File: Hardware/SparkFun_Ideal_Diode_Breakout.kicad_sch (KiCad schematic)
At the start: 23 parts, among them J1 Conn_01x05, J2 Conn_01x05, Q1 BCM857BS-7-F, Q2 DMG2305UX, Q3 BCM857BS-7-F, Q4 DMG2305UX, Q5 BCM857BS-7-F, Q6 DMG2305UX, Q7 BCM857BS-7-F, Q8 DMG2305UX

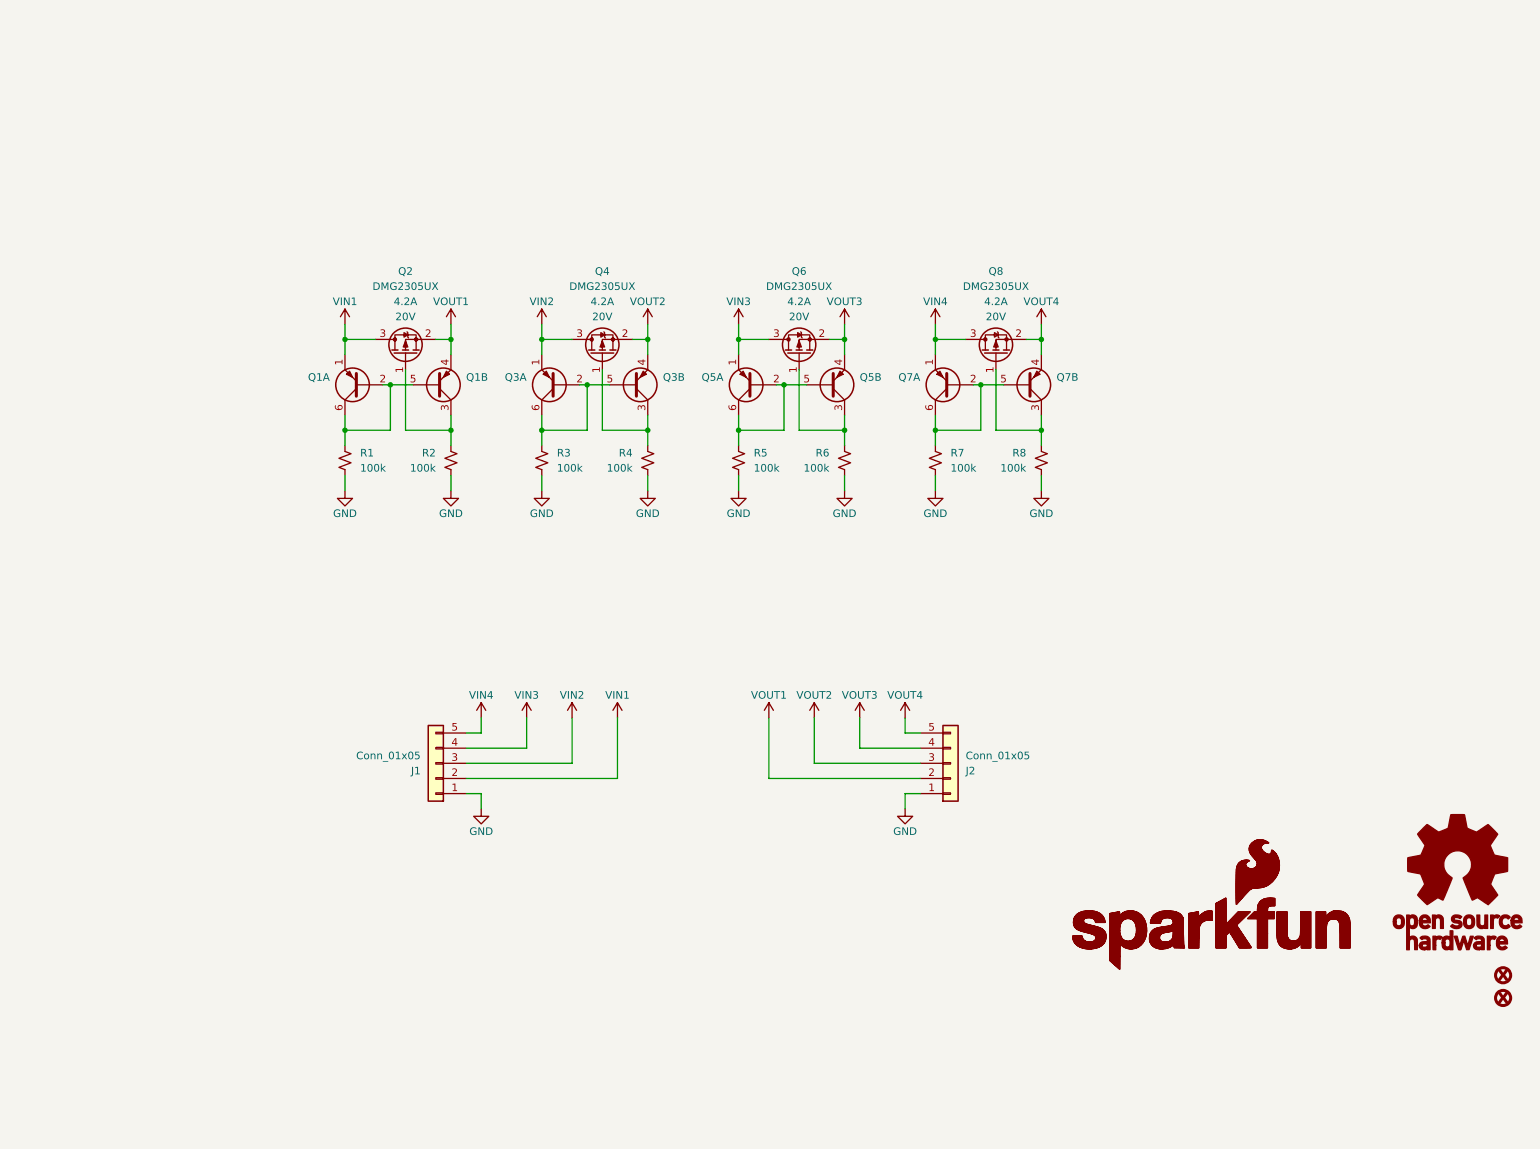
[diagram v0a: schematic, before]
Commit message: Design review updates
Update page info on schematic and board
Separate schematic sections with lines and header text
Add power ratings
Add diode symbols to schematic
Change GND symbol silk to "G"
Check and exclude ERC and DRC errors
Change top silk to "INx" and "Ox"
Change GND silk to inverted text
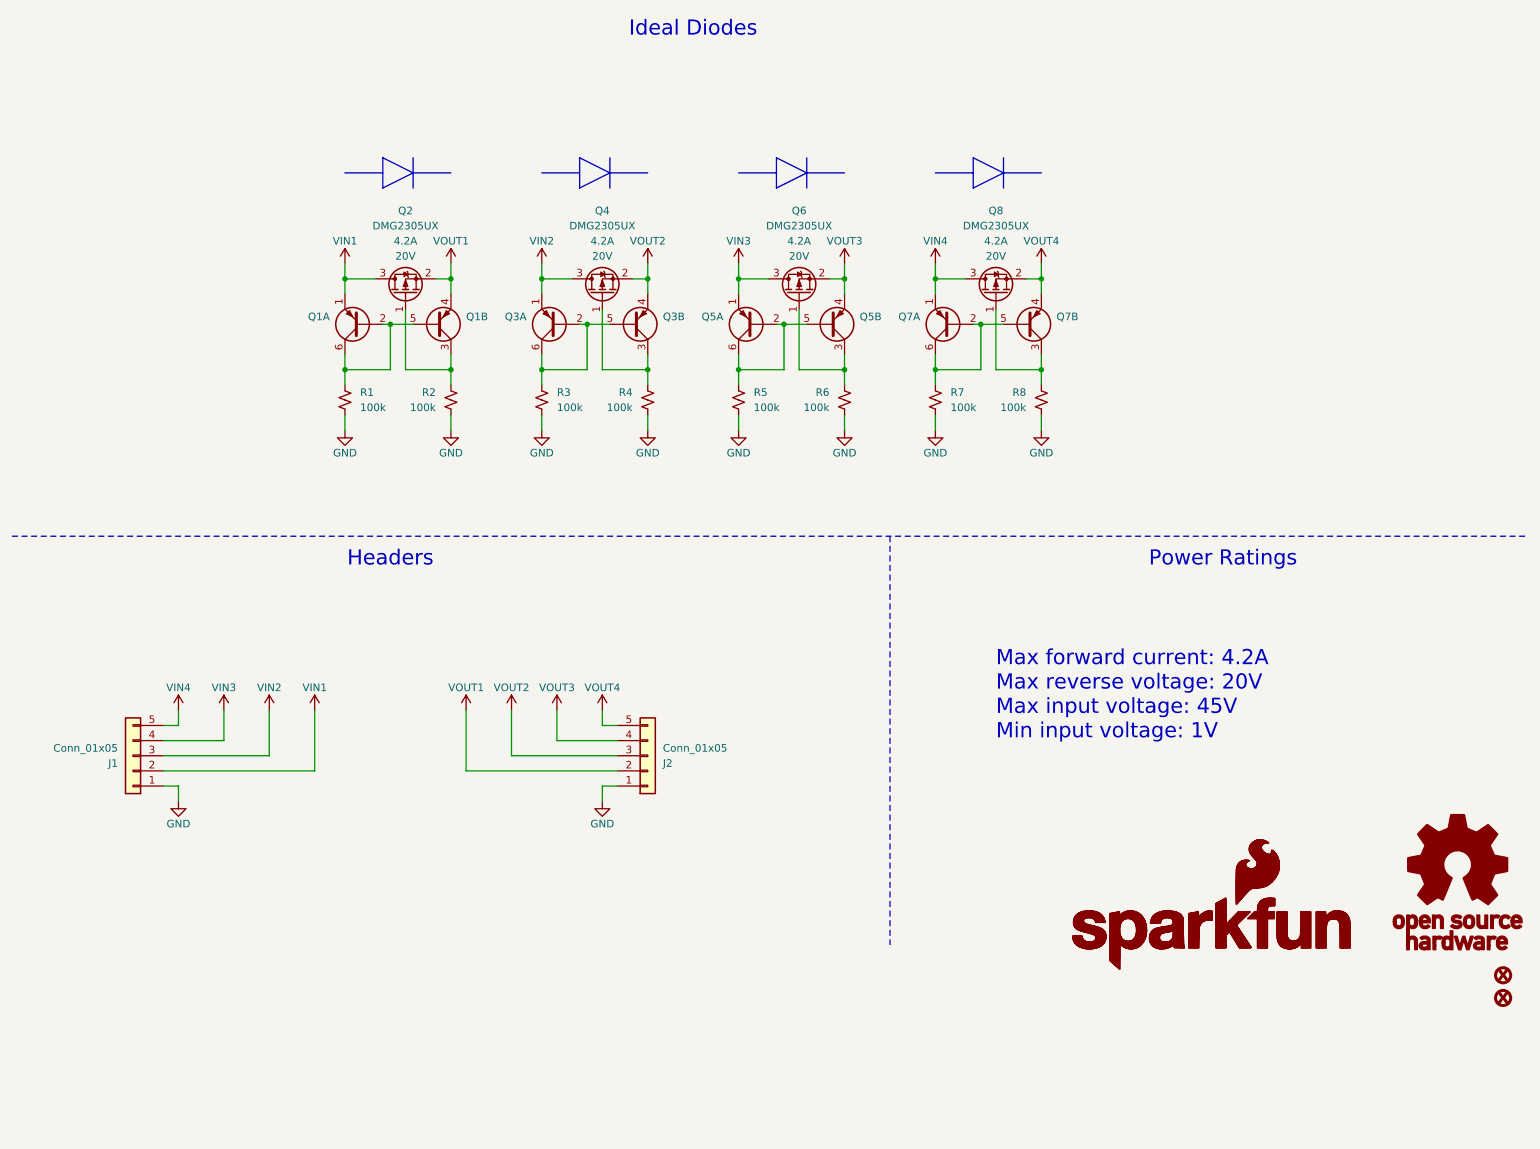
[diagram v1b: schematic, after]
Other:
- note added: "Headers"
- note added: "Ideal Diodes"
- note added: "Max forward current: 4.2A Max reverse voltage: 20V Max input voltage: 45V Min input voltage: 1V"
- note added: "Power Ratings"
- company: SparkFun -> SparkFun Electronics
- title: SparkFun Product (Qwiic) -> SparkFun Ideal Diode Breakout
- moved on the sheet: J1, J2, Q1A, Q1B, Q2, Q3A, Q3B, Q4, Q5A, Q5B, Q6, Q7A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

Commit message: Update ratings and add typical characteristics
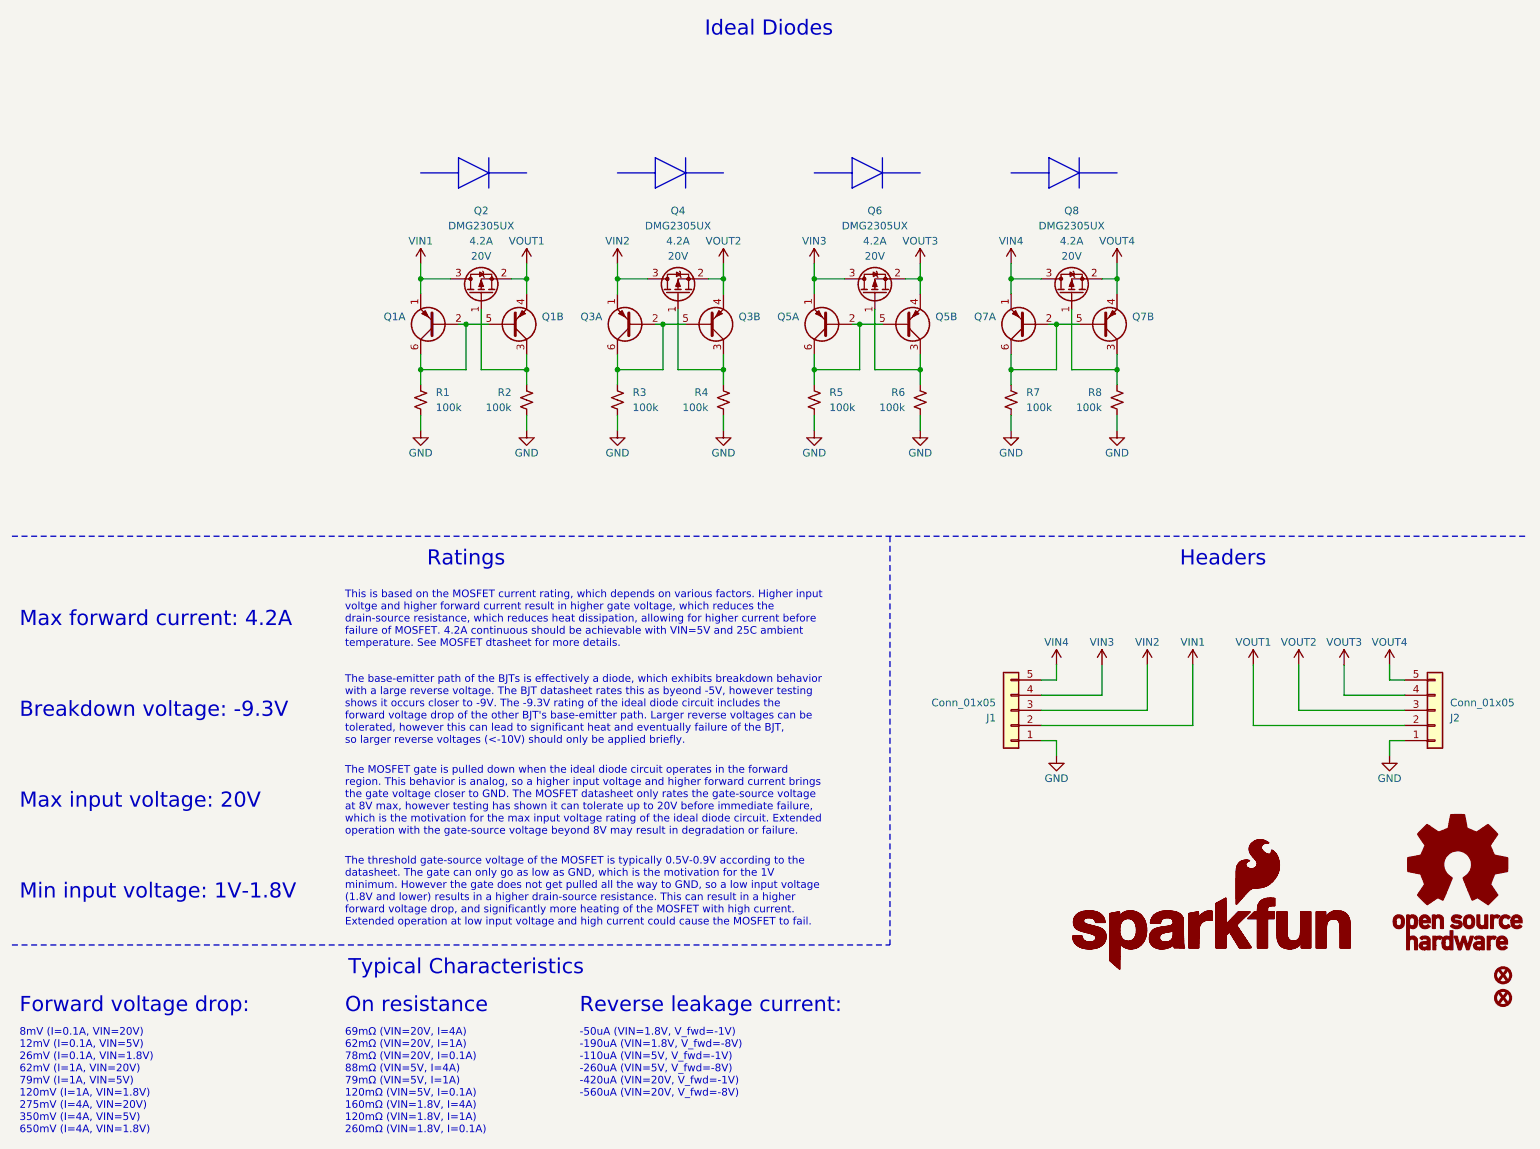
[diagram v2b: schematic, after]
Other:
- note added: "-50uA (VIN=1.8V, V_fwd=-1V) -190uA (VIN=1.8V, V_fwd=-8V) -110uA (VIN=5V, V_fwd=-1V) -260uA (VIN=5V, V_fwd=-8V) -420uA (VIN=20V, V_fwd=-1V) -560uA (VIN=20V, V_fwd=-8V)"
- note added: "69mΩ (VIN=20V, I=4A) 62mΩ (VIN=20V, I=1A) 78mΩ (VIN=20V, I=0.1A) 88mΩ (VIN=5V, I=4A) 79mΩ (VIN=5V, I=1A) 120mΩ (VIN=5V, I=0.1A) 160mΩ (VIN=1.8V, I=4A) 120mΩ (VIN=1.8V, I=1A) 260mΩ (VIN=1.8V, I=0.1A)"
- note added: "8mV (I=0.1A, VIN=20V) 12mV (I=0.1A, VIN=5V) 26mV (I=0.1A, VIN=1.8V) 62mV (I=1A, VIN=20V) 79mV (I=1A, VIN=5V) 120mV (I=1A, VIN=1.8V) 275mV (I=4A, VIN=20V) 350mV (I=4A, VIN=5V) 650mV (I=4A, VIN=1.8V)"
- note added: "Breakdown voltage: -9.3V"
- note added: "Forward voltage drop:"
- note added: "Max forward current: 4.2A"
- note added: "Max input voltage: 20V"
- note added: "Min input voltage: 1V-1.8V"
- note added: "On resistance"
- note added: "Ratings"
- note added: "Reverse leakage current:"
- note added: "The MOSFET gate is pulled down when the ideal diode circuit operates in the forward region. This behavior is analog, so a higher input voltage and higher forward current brings the gate voltage closer to GND. The MOSFET datasheet only rates the gate-source voltage at 8V max, however testing has shown it can tolerate up to 20V before immediate failure, which is the motivation for the max input vol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"
- note added: "The base-emitter path of the BJTs is effectively a diode, which exhibits breakdown behavior with a large reverse voltage. The BJT datasheet rates this as byeond -5V, however testing shows it occurs closer to -9V. The -9.3V rating of the ideal diode circuit includes the forward voltage drop of the other BJT's base-emitter path. Larger reverse voltages can be tolerated, however this can lead to sig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"
- note added: "The threshold gate-source voltage of the MOSFET is typically 0.5V-0.9V according to the datasheet. The gate can only go as low as GND, which is the motivation for the 1V minimum. However the gate does not get pulled all the way to GND, so a low input voltage (1.8V and lower) results in a higher drain-source resistance. This can result in a higher forward voltage drop, and significantly more heati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"
- note added: "This is based on the MOSFET current rating, which depends on various factors. Higher input voltge and higher forward current result in higher gate voltage, which reduces the drain-source resistance, which reduces heat dissipation, allowing for higher current before failure of MOSFET. 4.2A continuous should be achievable with VIN=5V and 25C ambient temperature. See MOSFET dtasheet for more details."
- note added: "Typical Characteristics"
- note removed: "Max forward current: 4.2A Max reverse voltage: 20V Max input voltage: 45V Min input voltage: 1V"
- note removed: "Power Ratings"
- moved on the sheet: J1, J2, Q1A, Q1B, Q2, Q3A, Q3B, Q4, Q5A, Q5B, Q6, Q7A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
